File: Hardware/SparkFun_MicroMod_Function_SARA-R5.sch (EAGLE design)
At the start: 99 parts, among them J1 MICROMOD_FUNCTION_STANDARD, J2 U.FL, J4 U.FL, J9 NANO_SIM, Q2 310mA/60V/1.6Ω, Q3 310mA/60V/1.6Ω, Q5 310mA/60V/1.6Ω, Q6 310mA/60V/1.6Ω, U1 SARA-R510M8S, U11 74HC1G04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

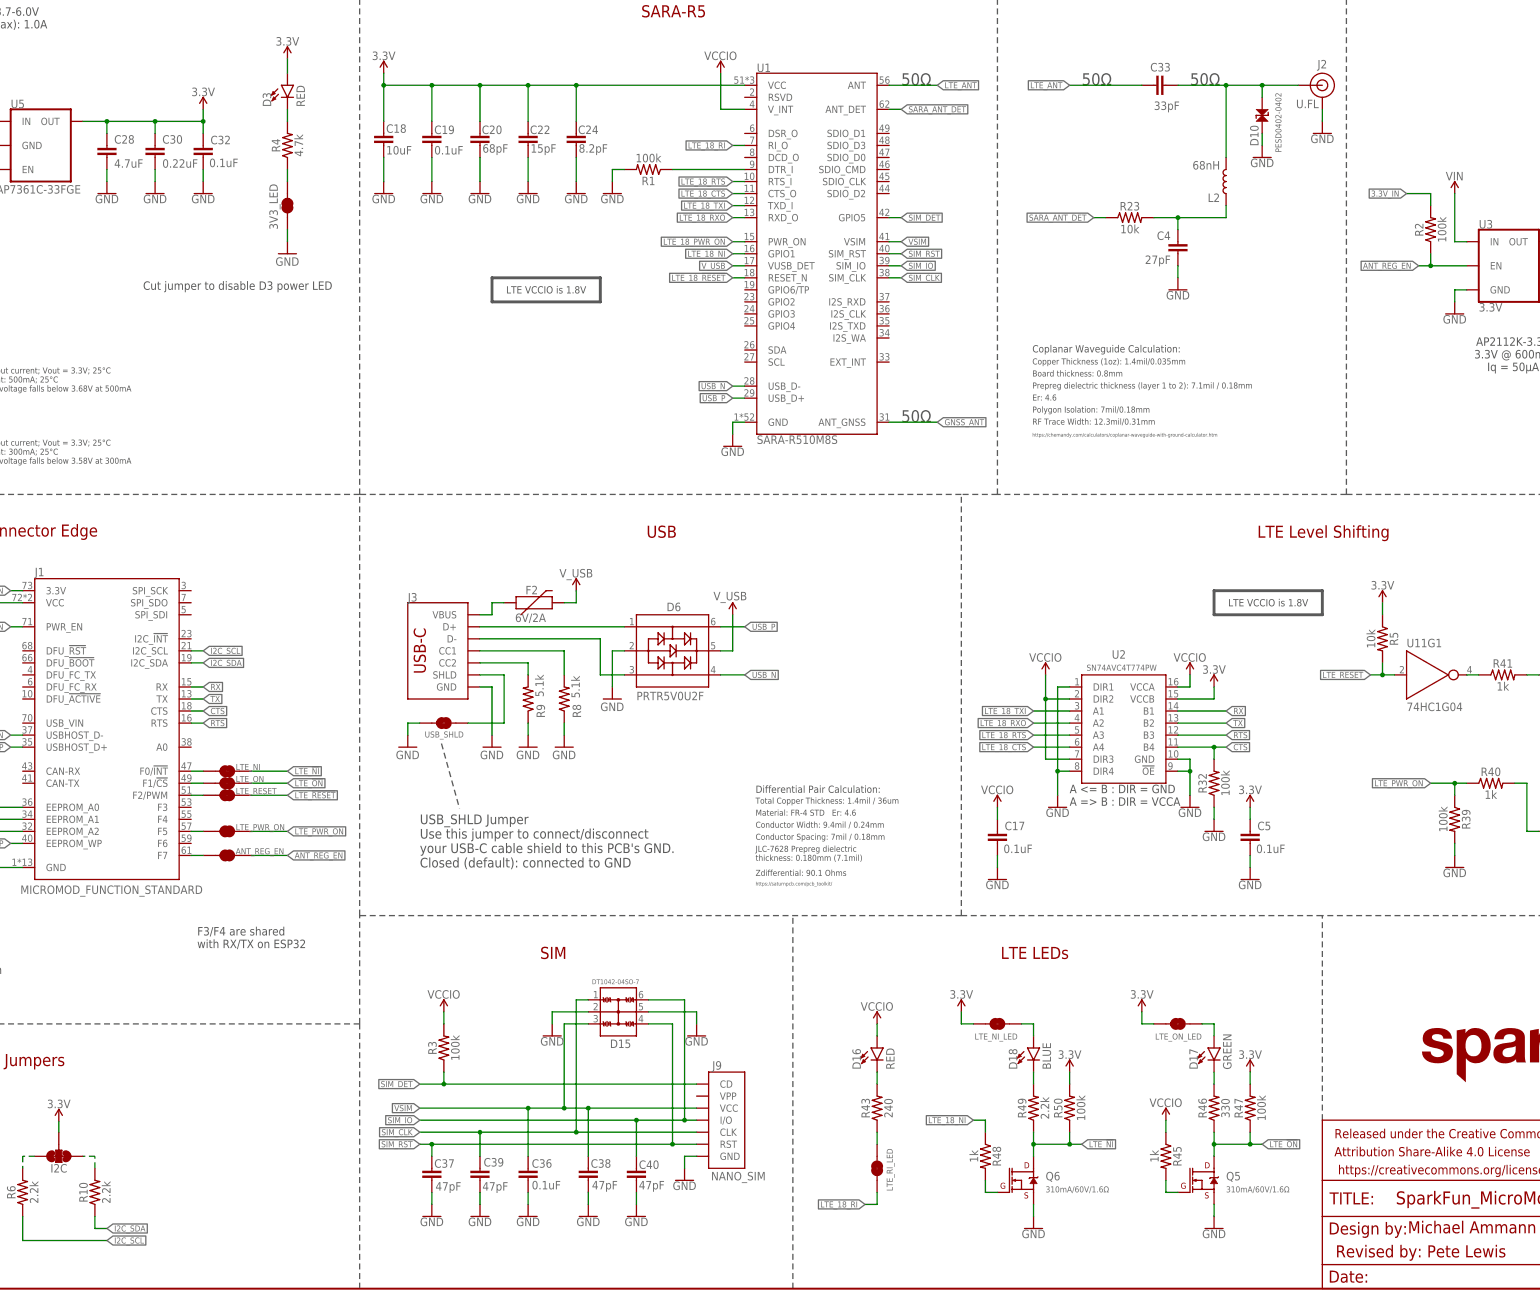
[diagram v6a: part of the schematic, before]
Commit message: Eng run checklist
-Minor schematic cleanup and tightening
-added some jumper text objects to sch
-added layer 1/2/3/4 text to copper layers
-switched to larger TP
-bumper version to v10
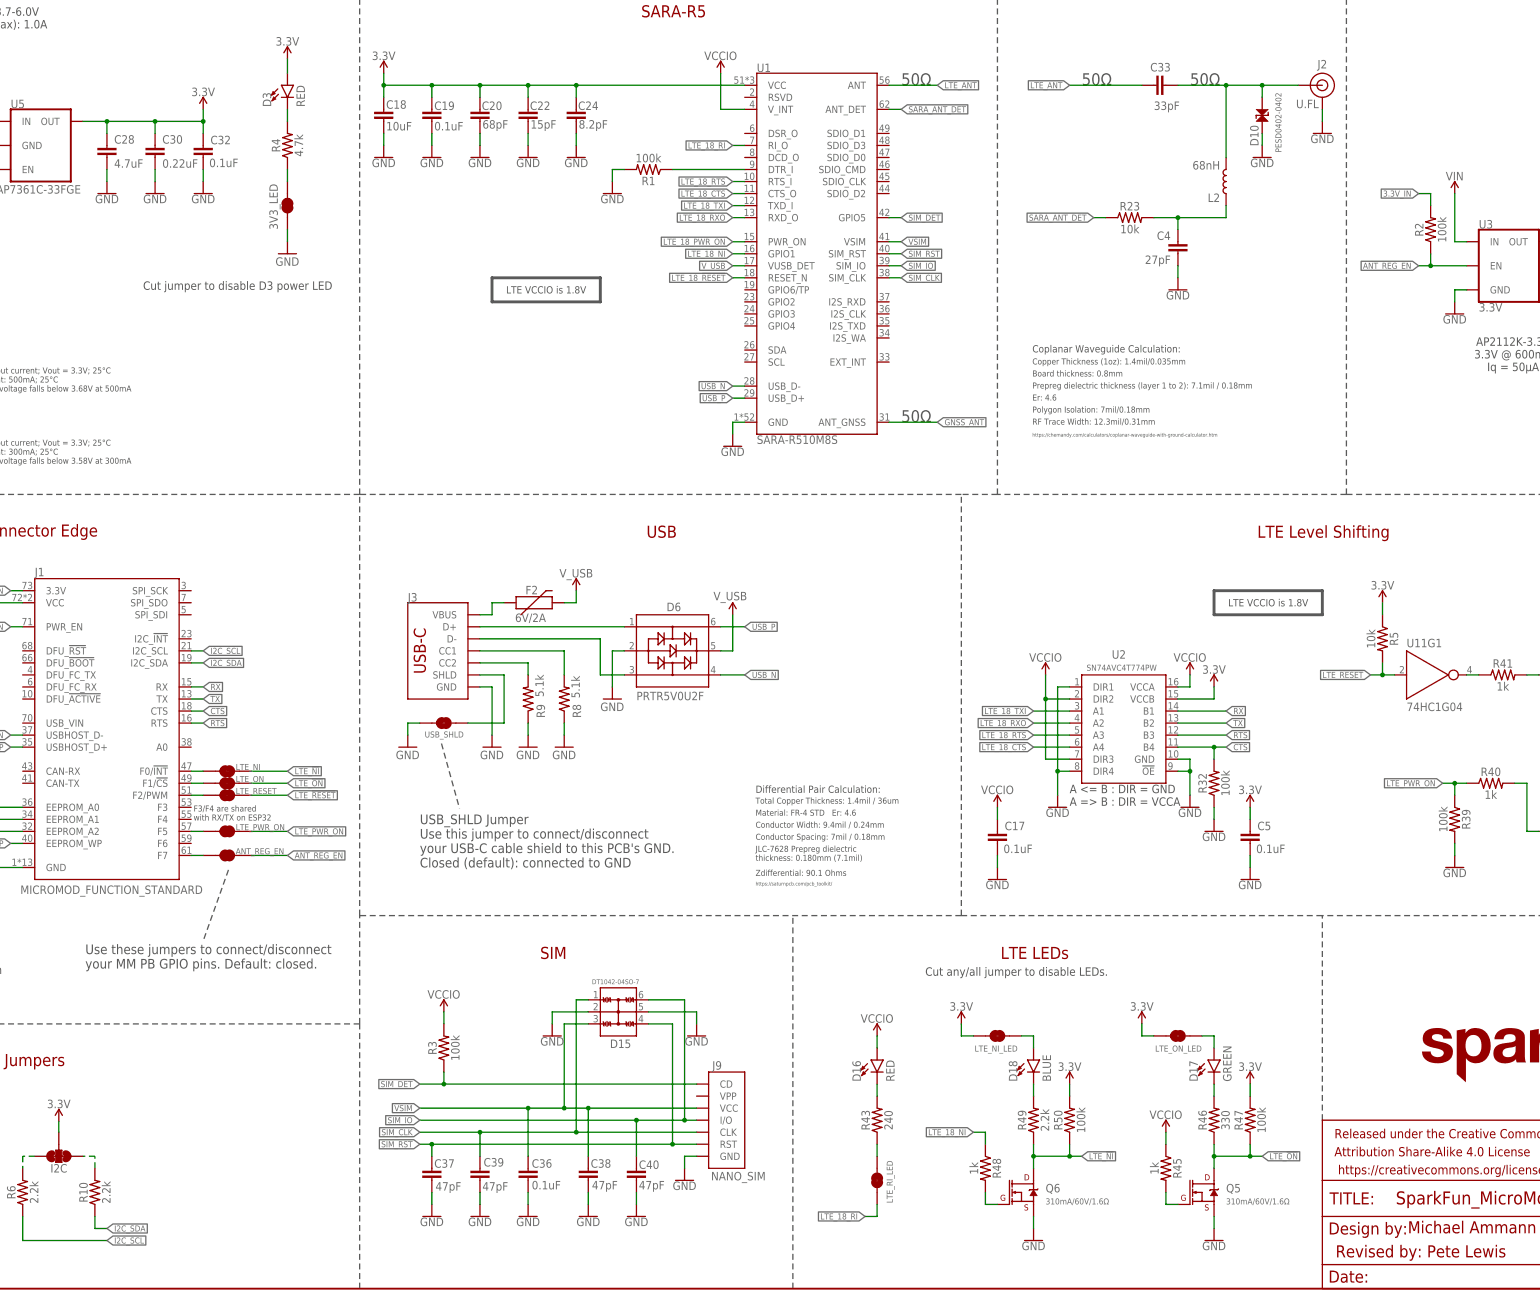
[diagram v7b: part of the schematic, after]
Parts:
- TP22: value TEST-POINT3 -> TEST-POINT3X4; device SparkFun-Connectors:TEST-POINT3 -> SparkFun-Connectors:TEST-POINT3X4
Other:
- note added: "Cut any/all jumper to disable LEDs."
- note added: "Use these jumpers to connect/disconnect your MM PB GPIO pins. Default: closed."
- moved on the sheet: C18, C19, C20, C22, C24, D16, D17, D18, LTE_NI_LED, LTE_ON_LED, LTE_RI_LED, Q5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

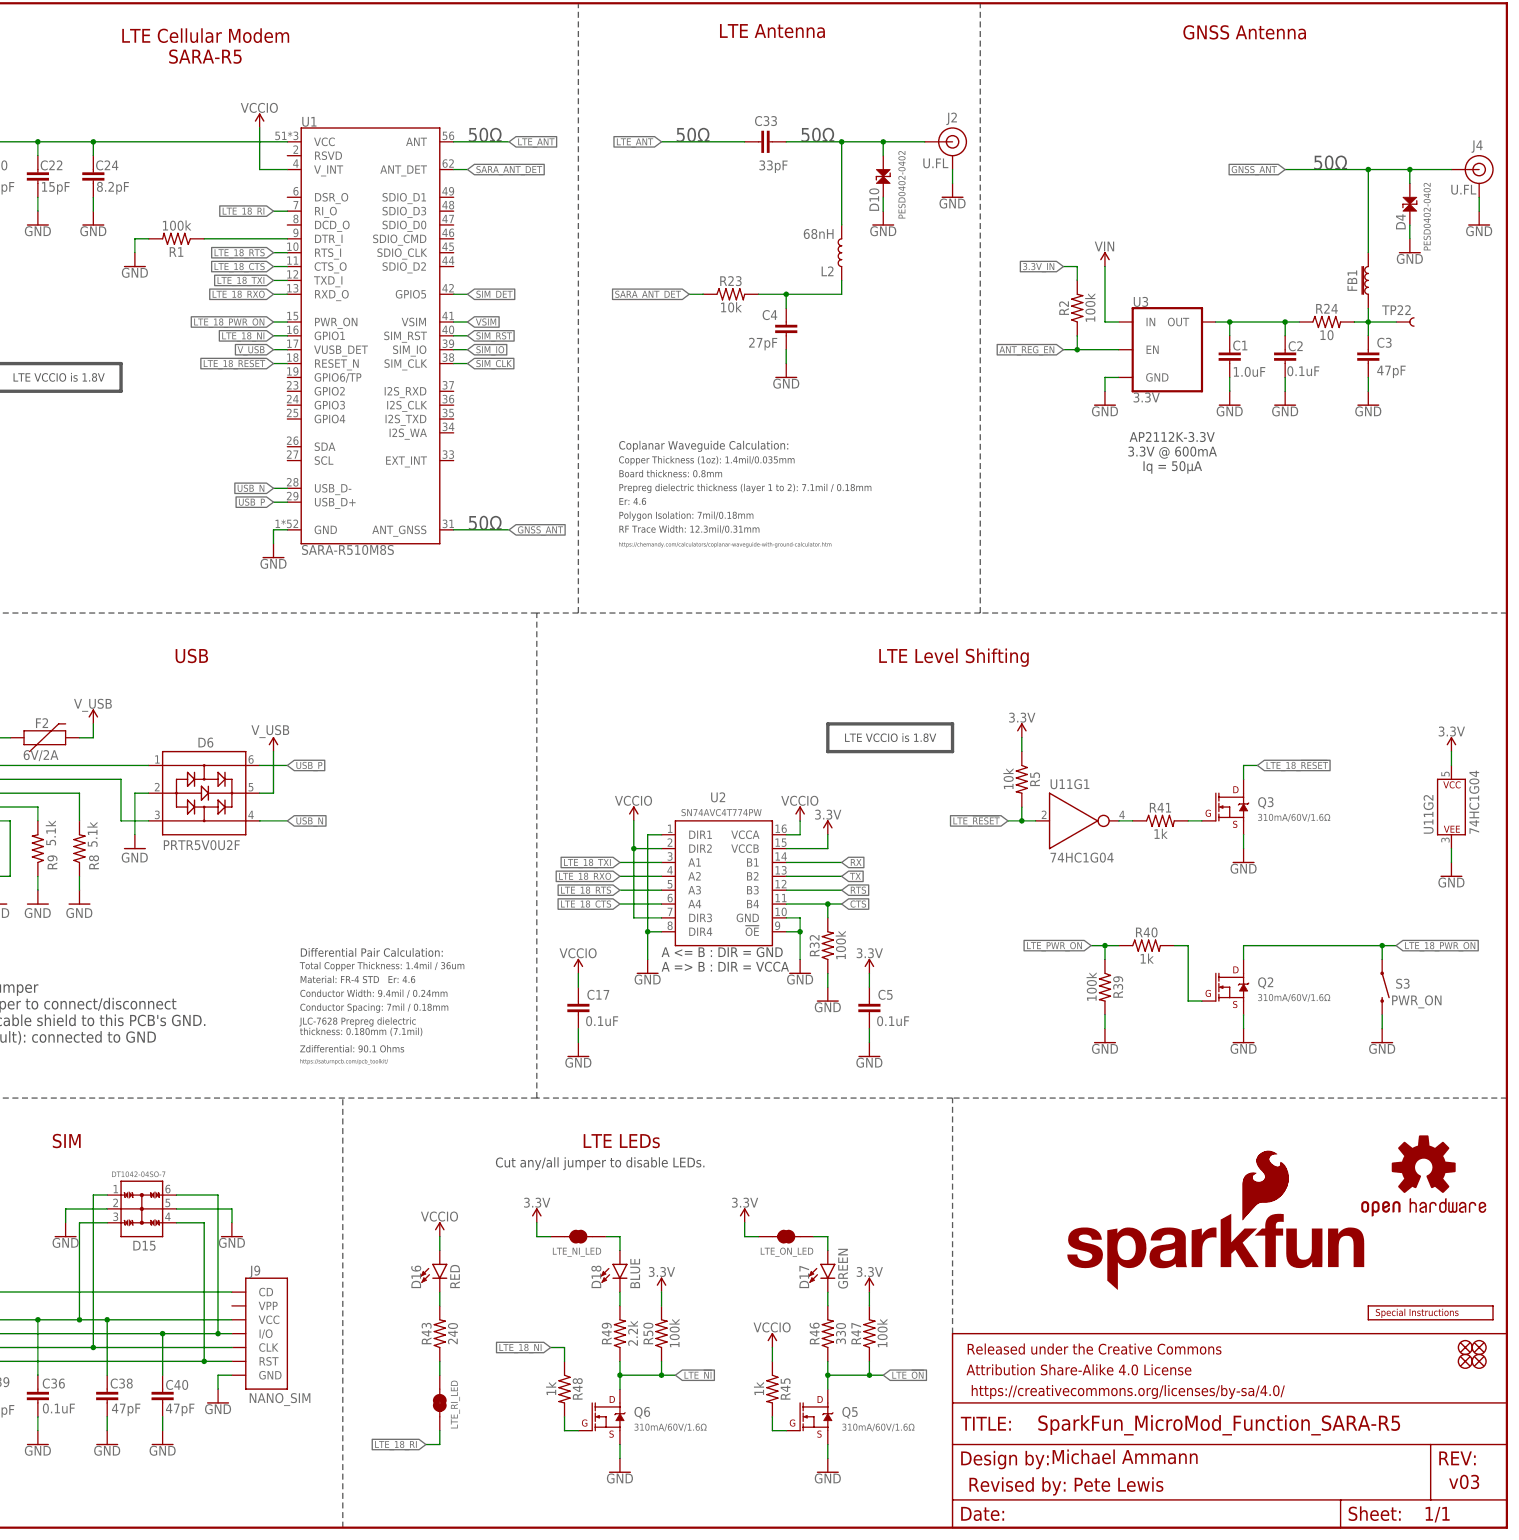
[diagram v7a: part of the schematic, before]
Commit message: minor sch aesthetic updates
-changed one V_USB flag to a power symbol
-updated version in s SCH to v10
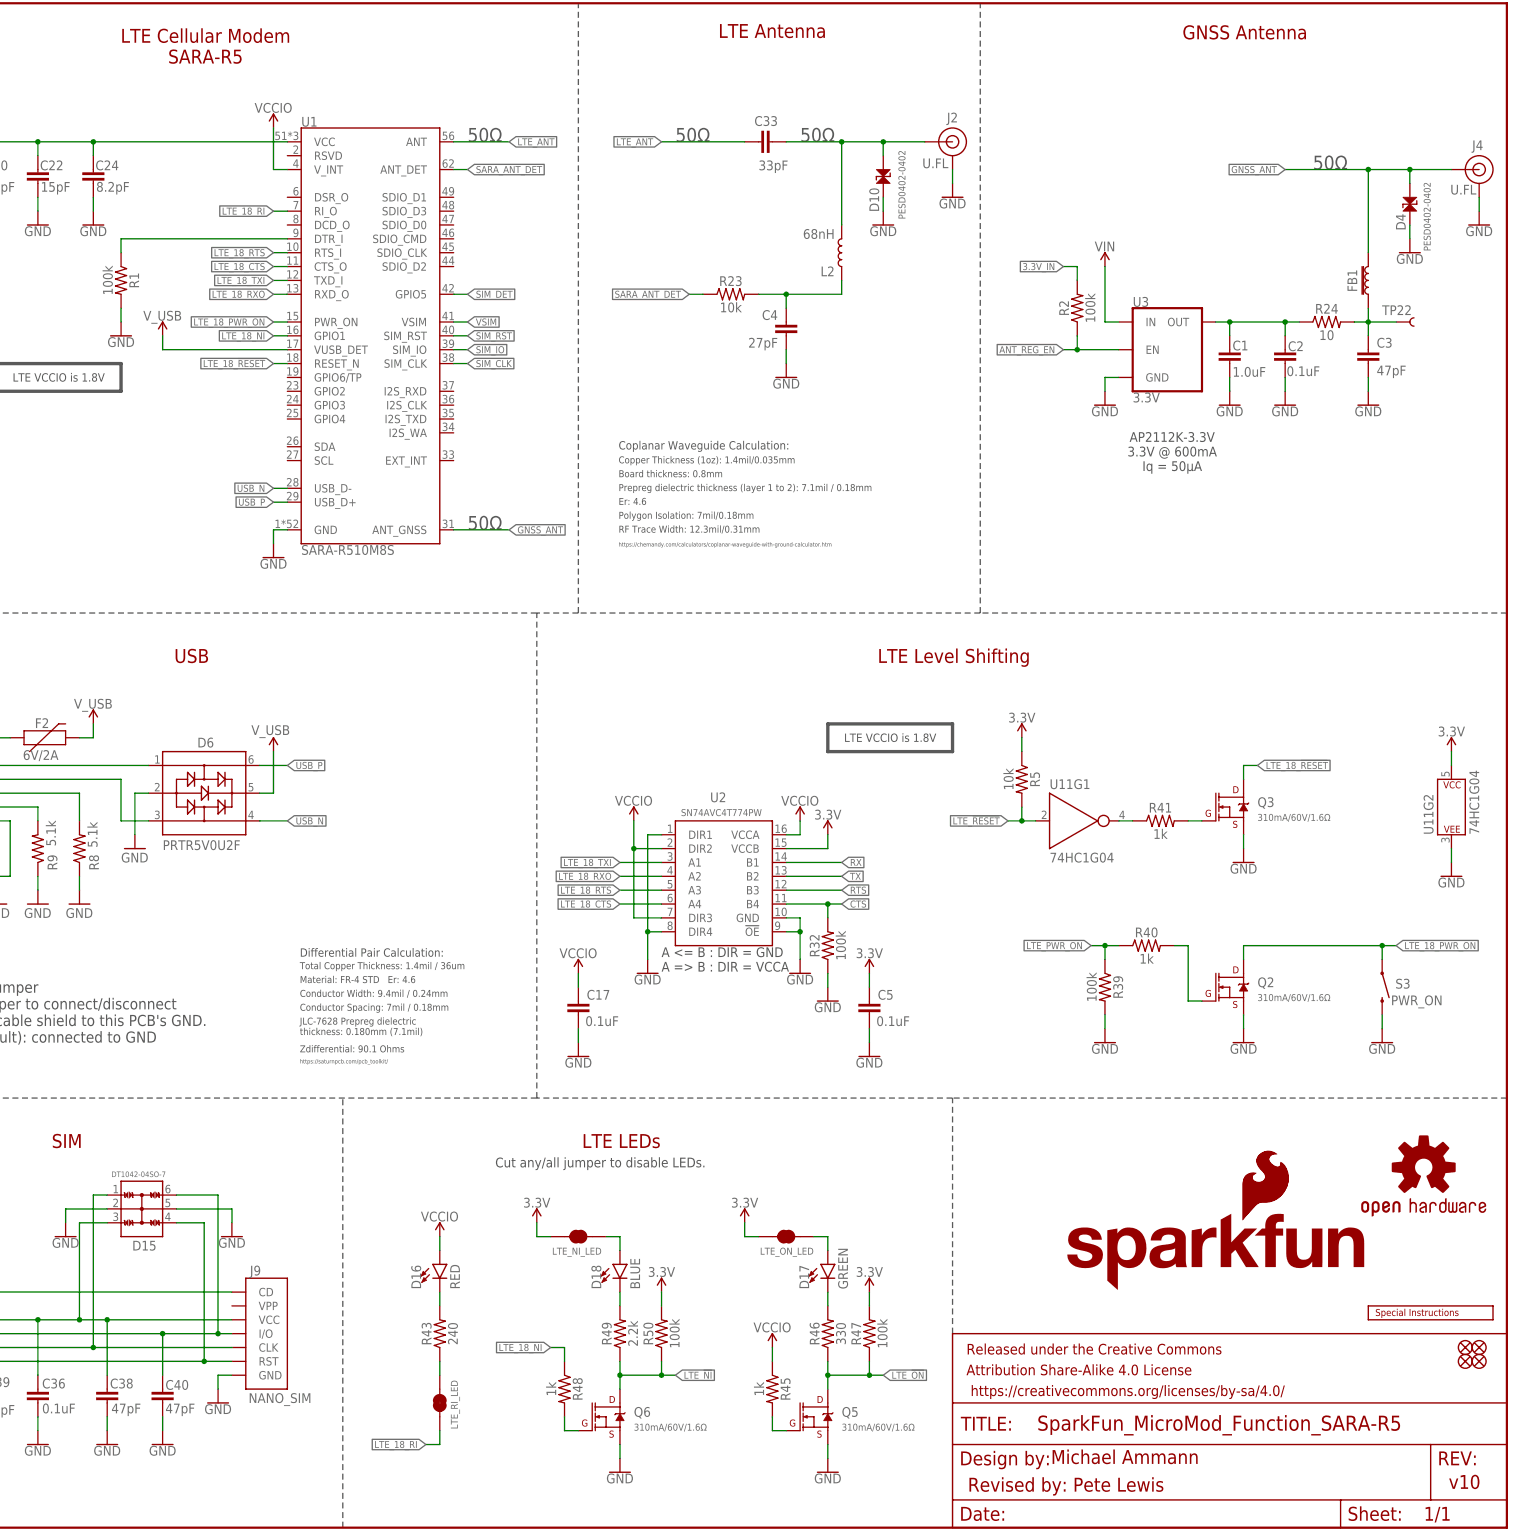
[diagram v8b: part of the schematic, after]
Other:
- note added: "v10"
- note removed: "v03"
- moved on the sheet: R1
